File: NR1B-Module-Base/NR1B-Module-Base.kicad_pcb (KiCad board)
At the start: 2 copper layers, 70.5 x 134 mm, 1 part, among them X1 NUCLEO144-ZIO

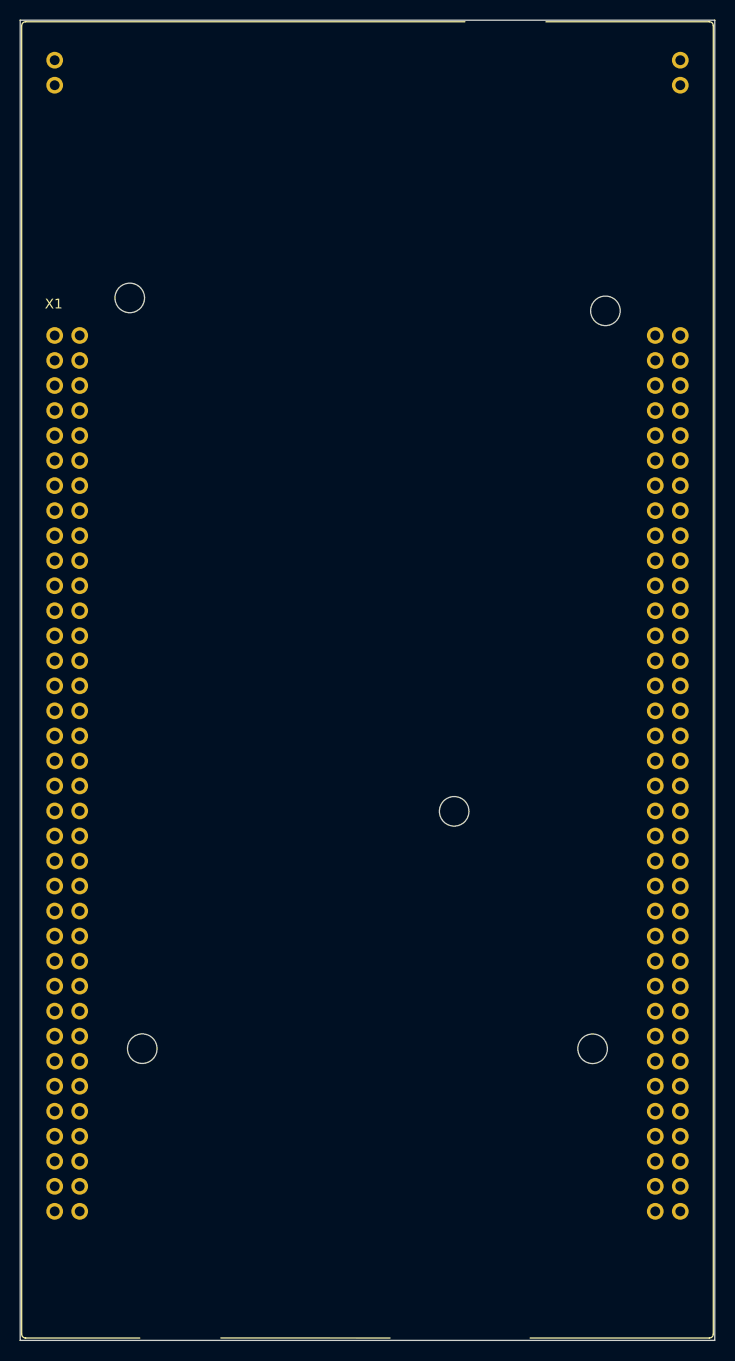
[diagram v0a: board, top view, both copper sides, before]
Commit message: Added two 2x4 pin header feedthrough connectors for non-MCU signals
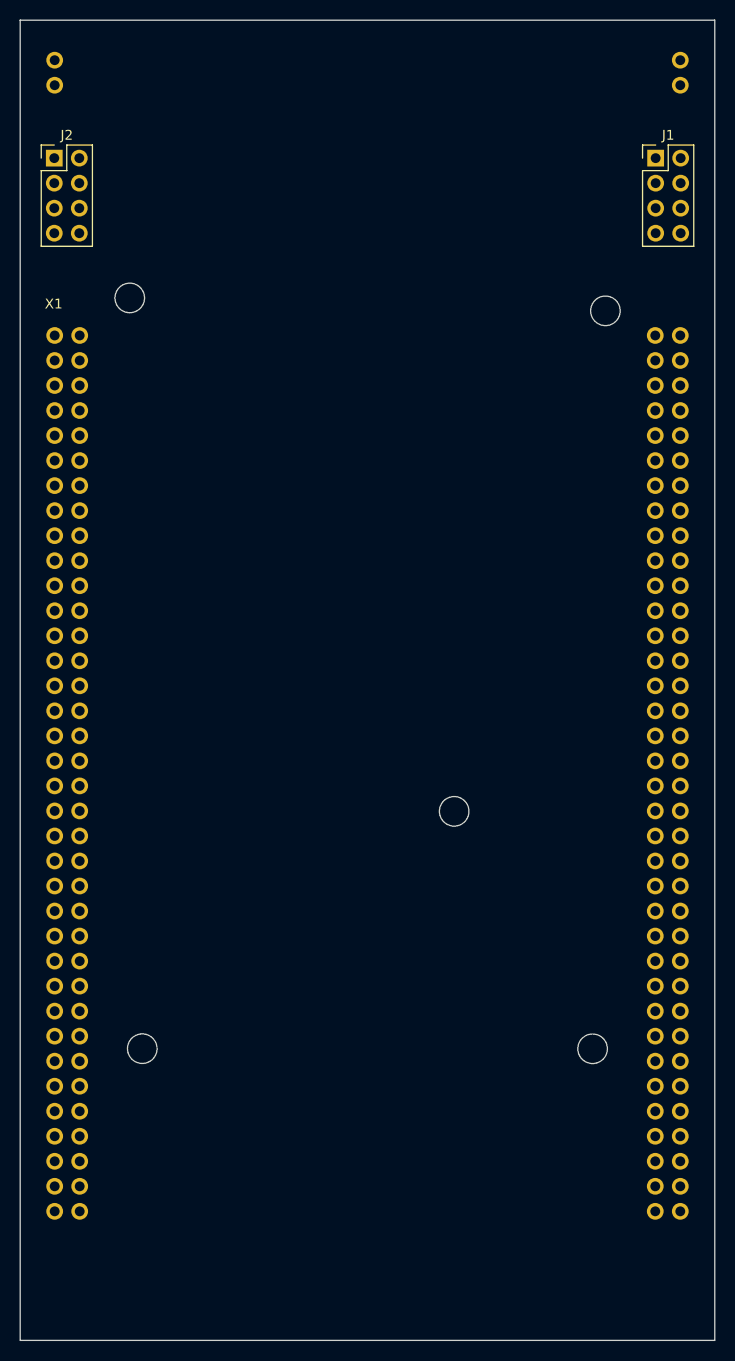
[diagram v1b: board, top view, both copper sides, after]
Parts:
- added J1: Conn_02x04_Odd_Even, Connector_PinHeader_2.54mm:PinHeader_2x04_P2.54mm_Vertical, F.Cu at (224.0, 94.0)
- added J2: Conn_02x04_Odd_Even, Connector_PinHeader_2.54mm:PinHeader_2x04_P2.54mm_Vertical, F.Cu at (163.0, 94.0)
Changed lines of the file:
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@@
   (net 143 "unconnected-(X1-Pad143)")
   (net 144 "unconnected-(X1-Pad144)")
+  (net 145 "unconnected-(J1-Pad1)")
+  (net 146 "unconnected-(J1-Pad2)")
+  (net 147 "unconnected-(J1-Pad3)")
+  (net 148 "unconnected-(J1-Pad4)")
+  (net 149 "unconnected-(J1-Pad5)")
+  (net 150 "unconnected-(J1-Pad6)")
+  (net 151 "unconnected-(J1-Pad7)")
+  (net 152 "unconnected-(J1-Pad8)")
+  (net 153 "unconnected-(J2-Pad1)")
+  (net 154 "unconnected-(J2-Pad2)")
+  (net 155 "unconnected-(J2-Pad3)")
+  (net 156 "unconnected-(J2-Pad4)")
+  (net 157 "unconnected-(J2-Pad5)")
+  (net 158 "unconnected-(J2-Pad6)")
+  (net 159 "unconnected-(J2-Pad7)")
+  (net 160 "unconnected-(J2-Pad8)")
+  (footprint "Connector_PinHeader_2.54mm:PinHeader_2x04_P2.54mm_Vertical" (layer "F.Cu")
+    (at 162.96 94)
+    (descr "Through hole straight pin header, 2x04, 2.54mm pitch, double rows")
+    (tags "Through hole pin header THT 2x04 2.54mm double row")
+    (property "Sheetfile" "NR1B-Module-Base.kicad_sch")
+    (property "Sheetname" "")
+    (attr through_hole)
+    (fp_text reference "J2" (at 1.27 -2.33) (layer "F.SilkS")
+      (effects (font (size 1 1) (thickness 0.15)))
+    )
+    (fp_text value "Conn_02x04_Odd_Even" (at 1.27 9.95) (layer "F.Fab")
+      (effects (font (size 1 1) (thickness 0.15)))
+    )
+    (fp_text user "${REFERENCE}" (at 1.27 3.81 90) (layer "F.Fab")
+      (effects (font (size 1 1) (thickness 0.15)))
+    )
+    (fp_line (start 3.87 -1.33) (end 3.87 8.95) (layer "F.SilkS") (width 0.12))
+    (fp_line (start 1.27 -1.33) (end 3.87 -1.33) (layer "F.SilkS") (width 0.12))
+    (fp_line (start -1.33 0) (end -1.33 -1.33) (layer "F.SilkS") (width 0.12))
+    (fp_line (start -1.33 8.95) (end 3.87 8.95) (layer "F.SilkS") (width 0.12))
+    (fp_line (start -1.33 -1.33) (end 0 -1.33) (layer "F.SilkS") (width 0.12))
+    (fp_line (start -1.33 1.27) (end 1.27 1.27) (layer "F.SilkS") (width 0.12))
+    (fp_line (start -1.33 1.27) (end -1.33 8.95) (layer "F.SilkS") (width 0.12))
+    (fp_line (start 1.27 1.27) (end 1.27 -1.33) (layer "F.SilkS") (width 0.12))
+    (fp_line (start -1.8 9.4) (end 4.35 9.4) (layer "F.CrtYd") (width 0.05))
+    (fp_line (start 4.35 -1.8) (end -1.8 -1.8) (layer "F.CrtYd") (width 0.05))
+    (fp_line (start -1.8 -1.8) (end -1.8 9.4) (layer "F.CrtYd") (width 0.05))
+    (fp_line (start 4.35 9.4) (end 4.35 -1.8) (layer "F.CrtYd") (width 0.05))
+    (fp_line (start 3.81 8.89) (end -1.27 8.89) (layer "F.Fab") (width 0.1))
+    (fp_line (start -1.27 8.89) (end -1.27 0) (layer "F.Fab") (width 0.1))
+    (fp_line (start 3.81 -1.27) (end 3.81 8.89) (layer "F.Fab") (width 0.1))
+    (fp_line (start 0 -1.27) (end 3.81 -1.27) (layer "F.Fab") (width 0.1))
+    (fp_line (start -1.27 0) (end 0 -1.27) (layer "F.Fab") (width 0.1))
+    (pad "1" thru_hole rect locked (at 0 0) (size 1.7 1.7) (drill 1) (layers *.Cu *.Mask)
+      (net 153 "unconnected-(J2-Pad1)") (pinfunction "Pin_1") (pintype "passive"))
+    (pad "2" thru_hole oval (at 2.54 0) (size 1.7 1.7) (drill 1) (layers *.Cu *.Mask)
+      (net 154 "unconnected-(J2-Pad2)") (pinfunction "Pin_2") (pintype "passive"))
+    (pad "3" thru_hole oval (at 0 2.54) (size 1.7 1.7) (drill 1) (layers *.Cu *.Mask)
+      (net 155 "unconnected-(J2-Pad3)") (pinfunction "Pin_3") (pintype "passive"))
+    (pad "4" thru_hole oval (at 2.54 2.54) (size 1.7 1.7) (drill 1) (layers *.Cu *.Mask)
+      (net 156 "unconnected-(J2-Pad4)") (pinfunction "Pin_4") (pintype "passive"))
+    (pad "5" thru_hole oval (at 0 5.08) (size 1.7 1.7) (drill 1) (layers *.Cu *.Mask)
+      (net 157 "unconnected-(J2-Pad5)") (pinfunction "Pin_5") (pintype "passive"))
+    (pad "6" thru_hole oval (at 2.54 5.08) (size 1.7 1.7) (drill 1) (layers *.Cu *.Mask)
+      (net 158 "unconnected-(J2-Pad6)") (pinfunction "Pin_6") (pintype "passive"))
+    (pad "7" thru_hole oval (at 0 7.62) (size 1.7 1.7) (drill 1) (layers *.Cu *.Mask)
+      (net 159 "unconnected-(J2-Pad7)") (pinfunction "Pin_7") (pintype "passive"))
+    (pad "8" thru_hole oval (at 2.54 7.62) (size 1.7 1.7) (drill 1) (layers *.Cu *.Mask)
+      (net 160 "unconnected-(J2-Pad8)") (pinfunction "Pin_8") (pintype "passive"))
+    (model "${KICAD6_3DMODEL_DIR}/Connector_PinHeader_2.54mm.3dshapes/PinHeader_2x04_P2.54mm_Vertical.wrl"
+      (offset (xyz 0 0 0))
+      (scale (xyz 1 1 1))
+      (rotate (xyz 0 0 0))
+    )
+  )
   (footprint "NISoC-Socket:ST_Morpho_Connector_144_STLink_MountingHoles" (layer "F.Cu")
     (at 163 112)
@@
       (effects (font (size 1 1) (thickness 0.15)))
     )
-    (fp_line (start 34.04 101.76) (end 16.86 101.75) (layer "F.SilkS") (width 0.12))
-    (fp_line (start 8.64 101.76) (end -2.95 101.76) (layer "F.SilkS") (width 0.12))
-    (fp_line (start -3.35 -31.44) (end -3.35 101.36) (layer "F.SilkS") (width 0.12))
-    (fp_line (start 49.86 -31.84) (end 66.45 -31.84) (layer "F.SilkS") (width 0.12))
-    (fp_line (start 41.64 -31.84) (end -2.95 -31.84) (layer "F.SilkS") (width 0.12))
-    (fp_line (start 66.85 101.36) (end 66.85 -31.44) (layer "F.SilkS") (width 0.12))
-    (fp_line (start 48.26 101.76) (end 66.45 101.76) (layer "F.SilkS") (width 0.12))
-    (fp_arc (start -2.95 101.76) (mid -3.232843 101.642843) (end -3.35 101.36) (layer "F.SilkS") (width 0.12))
-    (fp_arc (start -3.35 -31.44) (mid -3.232843 -31.722843) (end -2.95 -31.84) (layer "F.SilkS") (width 0.12))
-    (fp_arc (start 66.45 -31.84) (mid 66.732843 -31.722843) (end 66.85 -31.44) (layer "F.SilkS") (width 0.12))
-    (fp_arc (start 66.85 101.36) (mid 66.732843 101.642843) (end 66.45 101.76) (layer "F.SilkS") (width 0.12))
     (fp_line (start 41.25 -32.24) (end 50.25 -32.24) (layer "F.CrtYd") (width 0.05))
     (fp_line (start 67.25 102.16) (end 48.65 102.16) (layer "F.CrtYd") (width 0.05))
@@
       (offset (xyz 0 0 0))
       (scale (xyz 1 1 1))
+      (rotate (xyz 0 0 0))
+    )
+  )
+  (footprint "Connector_PinHeader_2.54mm:PinHeader_2x04_P2.54mm_Vertical" (layer "F.Cu")
+    (at 224 94)
+    (descr "Through hole straight pin header, 2x04, 2.54mm pitch, double rows")
+    (tags "Through hole pin header THT 2x04 2.54mm double row")
+    (property "Sheetfile" "NR1B-Module-Base.kicad_sch")
+    (property "Sheetname" "")
+    (attr through_hole)
+    (fp_text reference "J1" (at 1.27 -2.33) (layer "F.SilkS")
+      (effects (font (size 1 1) (thickness 0.15)))
+    )
+    (fp_text value "Conn_02x04_Odd_Even" (at 1.27 9.95) (layer "F.Fab")
+      (effects (font (size 1 1) (thickness 0.15)))
+    )
+    (fp_text user "${REFERENCE}" (at 1.27 3.81 90) (layer "F.Fab")
+      (effects (font (size 1 1) (thickness 0.15)))
+    )
+    (fp_line (start -1.33 -1.33) (end 0 -1.33) (layer "F.SilkS") (width 0.12))
+    (fp_line (start -1.33 1.27) (end 1.27 1.27) (layer "F.SilkS") (width 0.12))
+    (fp_line (start 3.87 -1.33) (end 3.87 8.95) (layer "F.SilkS") (width 0.12))
+    (fp_line (start -1.33 8.95) (end 3.87 8.95) (layer "F.SilkS") (width 0.12))
+    (fp_line (start 1.27 -1.33) (end 3.87 -1.33) (layer "F.SilkS") (width 0.12))
+    (fp_line (start -1.33 0) (end -1.33 -1.33) (layer "F.SilkS") (width 0.12))
+    (fp_line (start -1.33 1.27) (end -1.33 8.95) (layer "F.SilkS") (width 0.12))
+    (fp_line (start 1.27 1.27) (end 1.27 -1.33) (layer "F.SilkS") (width 0.12))
+    (fp_line (start -1.8 9.4) (end 4.35 9.4) (layer "F.CrtYd") (width 0.05))
+    (fp_line (start 4.35 9.4) (end 4.35 -1.8) (layer "F.CrtYd") (width 0.05))
+    (fp_line (start 4.35 -1.8) (end -1.8 -1.8) (layer "F.CrtYd") (width 0.05))
+    (fp_line (start -1.8 -1.8) (end -1.8 9.4) (layer "F.CrtYd") (width 0.05))
+    (fp_line (start 3.81 -1.27) (end 3.81 8.89) (layer "F.Fab") (width 0.1))
+    (fp_line (start -1.27 8.89) (end -1.27 0) (layer "F.Fab") (width 0.1))
+    (fp_line (start -1.27 0) (end 0 -1.27) (layer "F.Fab") (width 0.1))
+    (fp_line (start 3.81 8.89) (end -1.27 8.89) (layer "F.Fab") (width 0.1))
+    (fp_line (start 0 -1.27) (end 3.81 -1.27) (layer "F.Fab") (width 0.1))
+    (pad "1" thru_hole rect locked (at 0 0) (size 1.7 1.7) (drill 1) (layers *.Cu *.Mask)
+      (net 145 "unconnected-(J1-Pad1)") (pinfunction "Pin_1") (pintype "passive"))
+    (pad "2" thru_hole oval (at 2.54 0) (size 1.7 1.7) (drill 1) (layers *.Cu *.Mask)
+      (net 146 "unconnected-(J1-Pad2)") (pinfunction "Pin_2") (pintype "passive"))
+    (pad "3" thru_hole oval (at 0 2.54) (size 1.7 1.7) (drill 1) (layers *.Cu *.Mask)
+      (net 147 "unconnected-(J1-Pad3)") (pinfunction "Pin_3") (pintype "passive"))
+    (pad "4" thru_hole oval (at 2.54 2.54) (size 1.7 1.7) (drill 1) (layers *.Cu *.Mask)
+      (net 148 "unconnected-(J1-Pad4)") (pinfunction "Pin_4") (pintype "passive"))
+    (pad "5" thru_hole oval (at 0 5.08) (size 1.7 1.7) (drill 1) (layers *.Cu *.Mask)
+      (net 149 "unconnected-(J1-Pad5)") (pinfunction "Pin_5") (pintype "passive"))
+    (pad "6" thru_hole oval (at 2.54 5.08) (size 1.7 1.7) (drill 1) (layers *.Cu *.Mask)
+      (net 150 "unconnected-(J1-Pad6)") (pinfunction "Pin_6") (pintype "passive"))
+    (pad "7" thru_hole oval (at 0 7.62) (size 1.7 1.7) (drill 1) (layers *.Cu *.Mask)
+      (net 151 "unconnected-(J1-Pad7)") (pinfunction "Pin_7") (pintype "passive"))
+    (pad "8" thru_hole oval (at 2.54 7.62) (size 1.7 1.7) (drill 1) (layers *.Cu *.Mask)
+      (net 152 "unconnected-(J1-Pad8)") (pinfunction "Pin_8") (pintype "passive"))
+    (model "${KICAD6_3DMODEL_DIR}/Connector_PinHeader_2.54mm.3dshapes/PinHeader_2x04_P2.54mm_Vertical.wrl"
+      (offset (xyz 0 0 0))
+      (scale (xyz 1 1 1))
